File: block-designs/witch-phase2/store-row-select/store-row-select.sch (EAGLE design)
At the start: 13 parts, among them IC1 74LVC1G125DBV, Q1 MMBT2907ALT1SMD

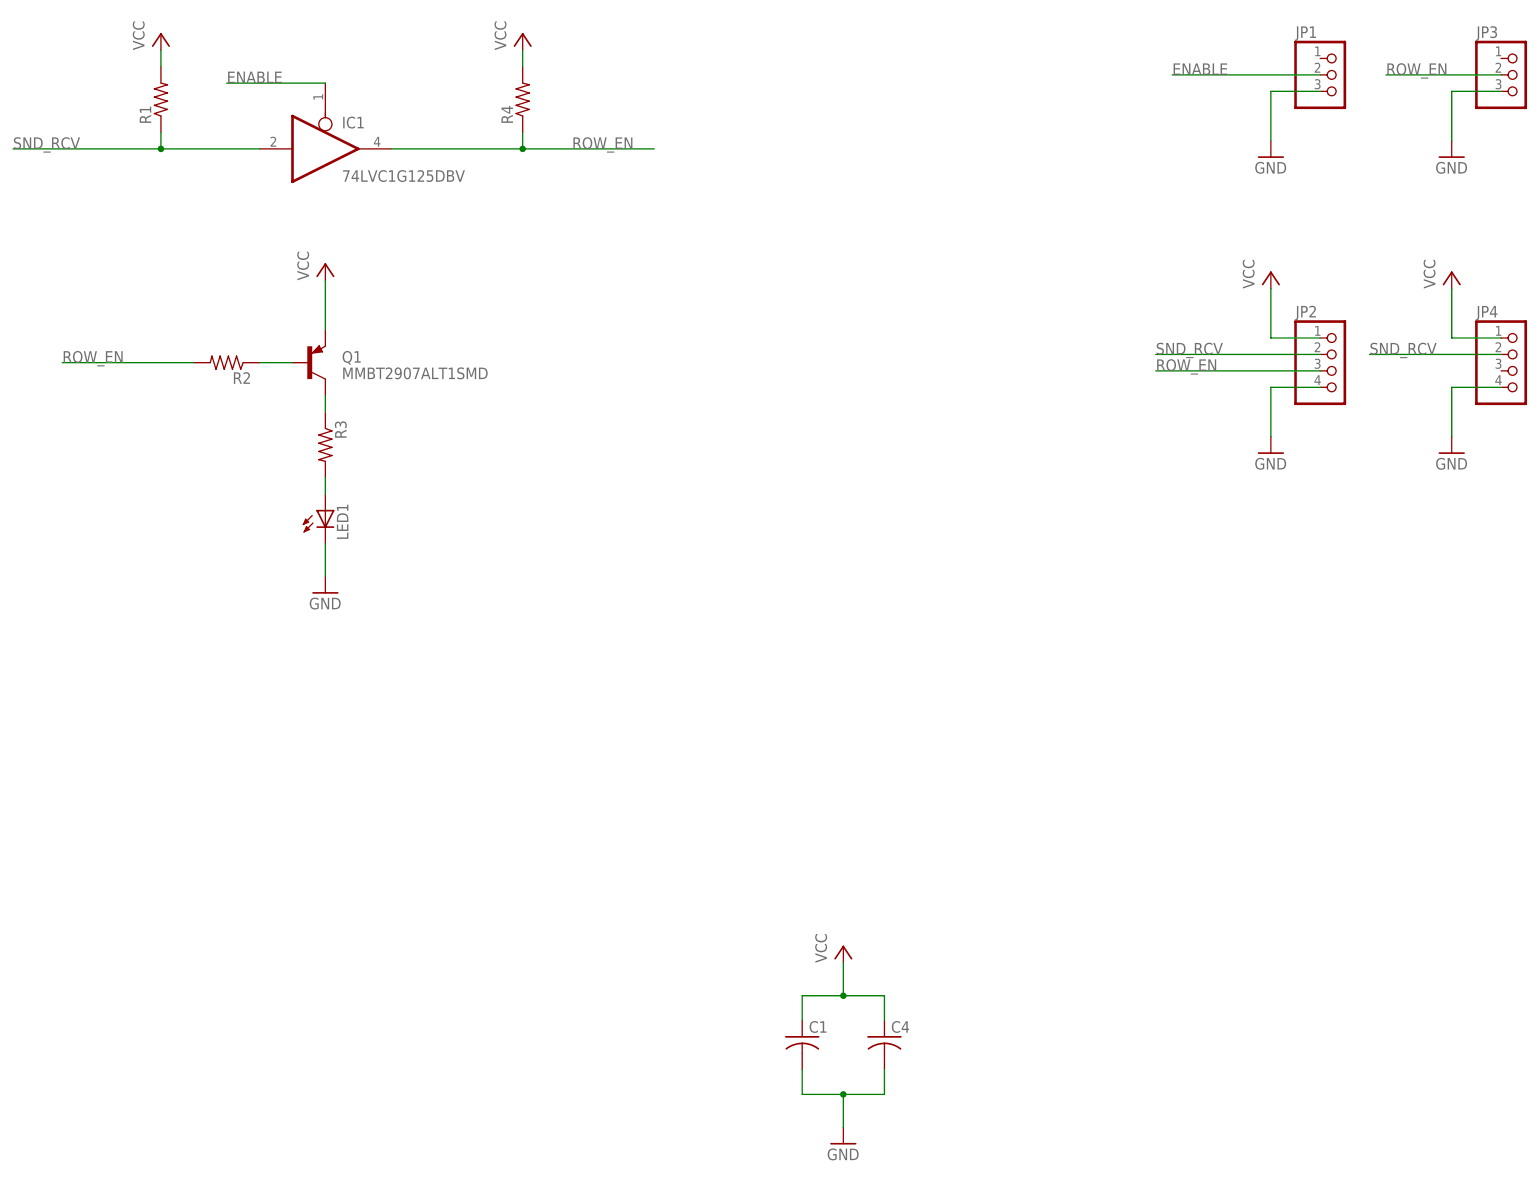
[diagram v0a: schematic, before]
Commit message: updated designs for new labeling and spacing
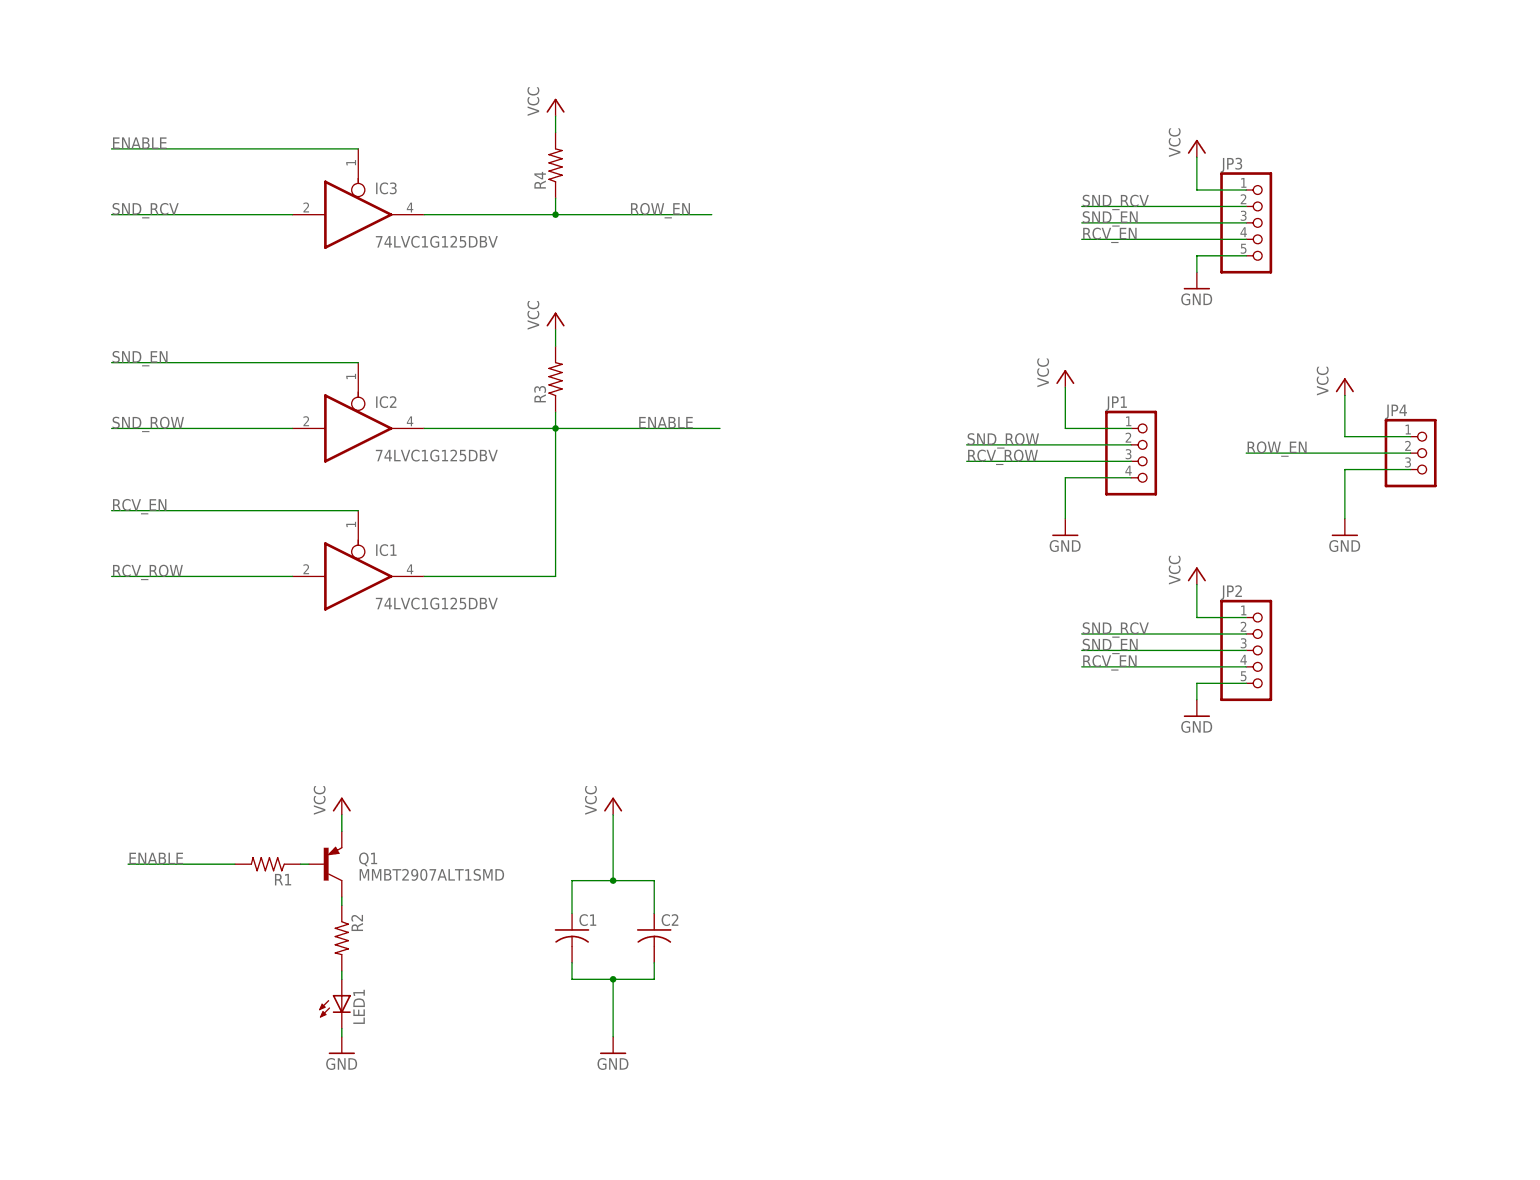
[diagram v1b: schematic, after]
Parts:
- removed C4: (no value), resistor:C-USC0805
- added C2: (no value), resistor:C-USC0805
- added IC2, IC3: 74LVC1G125DBV, 74xx-little-us:74LVC1G125DBV
- JP1: device pinhead:PINHD-1X3 -> pinhead:PINHD-1X4
- JP2: device pinhead:PINHD-1X4 -> pinhead:PINHD-1X5
- JP3: device pinhead:PINHD-1X3 -> pinhead:PINHD-1X5
- JP4: device pinhead:PINHD-1X4 -> pinhead:PINHD-1X3
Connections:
- new net RCV_EN: IC1A.OE, JP2.4, JP3.4
- new net RCV_ROW: IC1A.I, JP1.3
- new net SND_EN: IC2A.OE, JP2.3, JP3.3
- new net SND_ROW: IC2A.I, JP1.2
- net ENABLE: now also IC1A.O, IC2A.O, IC3A.OE, R1.2, R3.1; no longer IC1A.OE, JP1.2
- net GND: now also C2.2, JP1.4, JP2.5, JP3.5, JP4.3; no longer C4.2, JP1.3, JP2.4, JP3.3, JP4.4
- net N$2: now also R1.1; no longer R2.1
- net N$4: now also R2.1; no longer R3.1
- net N$5: now also R2.2; no longer R3.2
- net ROW_EN: now also IC3A.O, JP4.2; no longer IC1A.O, JP2.3, JP3.2, R2.2
- net SND_RCV: now also IC3A.I, JP3.2; no longer IC1A.I, JP4.2, R1.1
- net VCC: now also C2.1, JP1.1, JP3.1, R3.2; no longer C4.1, R1.2
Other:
- moved on the sheet: C1, IC1, LED1, Q1, R1, R2, R3, R4
